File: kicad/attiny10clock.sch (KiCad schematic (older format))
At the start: 45 parts, among them J1 USB_B, SW1 SW_DIP_x01, SW2 SW_DIP_x01, SW3 SW_DIP_x01, SW4 SW_DIP_x01, SW5 SW_DIP_x01, U1 ATtiny10-TS, U2 74HC595, U3 74HC595, U4 74LS247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

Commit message: use different footpritn for osc
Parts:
- X1: footprint Oscillator:Oscillator_SMD_Fordahl_DFAS15-4Pin_5.0x3.2mm -> random_stuff:ASFLK
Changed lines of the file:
@@
 F 0 "X1" H 1644 4296 50  0000 L CNN
 F 1 "DFA-S15" H 1644 4205 50  0000 L CNN
-F 2 "Oscillator:Oscillator_SMD_Fordahl_DFAS15-4Pin_5.0x3.2mm" H 2300 3900 50  0001 C CNN
+F 2 "random_stuff:ASFLK" H 2300 3900 50  0001 C CNN
 F 3 "http://www.metatech.com.hk/product/fordahl/pdf/2002%20TCXO%20Page%2043-58.pdf" H 1100 4250 50  0001 C CNN
 	1    1200 4250

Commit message: Rev 3 of schematic, start pcb
also new code rev
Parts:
- removed C10, C9: 100n, Capacitor_SMD:C_0805_2012Metric_Pad1.15x1.40mm_HandSolder, symbol Device:C
- removed R6: 270, Resistor_SMD:R_1210_3225Metric_Pad1.42x2.65mm_HandSolder, symbol Device:R
- removed U2, U3: 74HC595, Package_SO:SOIC-16_3.9x9.9mm_P1.27mm, symbol 74xx:74HC595
- removed U4, U5, U6, U7: 74LS247, Package_SO:SOIC-16_3.9x9.9mm_P1.27mm, symbol 74xx:74LS247
- added F1: 500ma, Fuse:Fuse_1206_3216Metric_Pad1.42x1.75mm_HandSolder, symbol Device:Fuse
- added J2: Conn_02x04_Odd_Even, Connector_PinHeader_2.54mm:PinHeader_2x04_P2.54mm_Vertical, symbol Connector_Generic:Conn_02x04_Odd_Even
- added U2, U3, U4, U5: NPIC6C595, Package_SO:TSSOP-16_4.4x5mm_P0.65mm, symbol random_things:NPIC6C595
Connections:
- net labels removed: hourha, hourhb, hourla, hourlb, hourlc, hourld, minha, minhb, minhc, minla, minlb, minlc, minld
- wire segments 120 -> 149
- no-connect marks 13 -> 10
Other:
- moved on the sheet: C11, C13, D1, D2, D3, R7, R8, R9, SW1

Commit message: Úse another buck converter
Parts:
- removed C11: 470p, Capacitor_SMD:C_0805_2012Metric_Pad1.15x1.40mm_HandSolder, symbol Device:C
- removed C12: 180u, Capacitor_THT:CP_Radial_D8.0mm_P3.50mm, symbol Device:CP
- removed C13: 100n, Capacitor_SMD:C_0805_2012Metric_Pad1.15x1.40mm_HandSolder, symbol Device:C
- removed C2: 1u, Capacitor_SMD:C_0805_2012Metric_Pad1.15x1.40mm_HandSolder, symbol Device:C
- removed C6: 100u, Capacitor_THT:CP_Radial_D8.0mm_P3.50mm, symbol Device:CP
- removed D7: D_Schottky, Diode_SMD:D_3220_8050Metric_Pad2.65x5.15mm_HandSolder, symbol Device:D_Schottky
- removed L1: 100u, Inductor_THT:L_Toroid_Vertical_L13.0mm_W6.5mm_P5.60mm, symbol Device:L
- removed R7: 150m, Resistor_THT:R_Axial_DIN0309_L9.0mm_D3.2mm_P12.70mm_Horizontal, symbol Device:R
- removed R8: 5k6, Resistor_SMD:R_0603_1608Metric_Pad1.05x0.95mm_HandSolder, symbol Device:R
- removed R9: 3k3, Resistor_SMD:R_0603_1608Metric_Pad1.05x0.95mm_HandSolder, symbol Device:R
- removed U8: MC34063AP, Package_DIP:DIP-8_W7.62mm, symbol Regulator_Switching:MC34063AP
- added C6, C9: 22u, Capacitor_SMD:C_0805_2012Metric_Pad1.15x1.40mm_HandSolder, symbol Device:C_Small
- added L1: 1.5u, Inductor_SMD:L_Wuerth_WE-PD-Typ-7345, symbol Device:L_Small
- added R6: 27k, Resistor_SMD:R_0603_1608Metric_Pad1.05x0.95mm_HandSolder, symbol Device:R_Small
- added R7: 12k, Resistor_SMD:R_0603_1608Metric_Pad1.05x0.95mm_HandSolder, symbol Device:R_Small
- added U6: RT8097AHGB, Package_TO_SOT_SMD:SOT-23-5_HandSoldering, symbol random_things:RT8097AHGB
- R1: value 100 -> 22k
- R2: value 300 -> 10k
- R3: value 1k -> 3k9
- R4: value 3k -> 1k2
- R5: value 1k -> 10k
- SW2, SW3, SW4, SW5: footprint Connector_PinHeader_2.54mm:PinHeader_1x02_P2.54mm_Vertical -> Button_Switch_Keyboard:SW_Cherry_MX_1.00u_Plate
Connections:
- net labels added: btn_in, clk, ser_clk, ser_in
- wire segments 149 -> 120
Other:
- note added: "buttons at \n1.5V, 2.5V, 3.5V 4.5V\n\nshould add thresholds at \n1V 2V 3V 4V\n\nneeds software debounce"
- moved on the sheet: C1, C3, C4, C5, C7, C8, D1, D2, D3, D4, D5, D6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

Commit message: Use new micro usb + more routing
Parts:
- removed J1: USB_B, Connector_USB:USB_B_OST_USB-B1HSxx_Horizontal, symbol Connector:USB_B
- added H1, H2, H3, H4: MountingHole, MountingHole:MountingHole_2.2mm_M2, symbol Mechanical:MountingHole
- added J1: USB_B_Micro, random_stuff:USB_MICRO_10118193-0001LF, symbol Connector:USB_B_Micro
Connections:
- wire segments 120 -> 118
- no-connect marks 10 -> 12
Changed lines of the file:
@@
-	1    0    0    -1
-$EndComp
-$Comp
-L Connector:USB_B J1
-U 1 1 6029C5DE
-P 1200 2750
-F 0 "J1" H 1257 3217 50  0000 C CNN
-F 1 "USB_B" H 1257 3126 50  0000 C CNN
-F 2 "Connector_USB:USB_B_OST_USB-B1HSxx_Horizontal" H 1350 2700 50  0001 C CNN
-F 3 " ~" H 1350 2700 50  0001 C CNN
-	1    1200 2750
 	1    0    0    -1
 $EndComp
@@
 	1    0    0    -1
 $EndComp
-Connection ~ 1200 3150
 Wire Wire Line
 	2500 2550 2500 2450
@@
 	1    0    0    -1
 $EndComp
-Wire Wire Line
-	1200 3150 1100 3150
-$Comp
-L power:GND #PWR0109
-U 1 1 602A0375
-P 1200 3200
-F 0 "#PWR0109" H 1200 2950 50  0001 C CNN
-F 1 "GND" H 1205 3027 50  0000 C CNN
-F 2 "" H 1200 3200 50  0001 C CNN
-F 3 "" H 1200 3200 50  0001 C CNN
-	1    1200 3200
-	1    0    0    -1
-$EndComp
-Wire Wire Line
-	1200 3200 1200 3150
 Wire Wire Line
 	8400 5450 8400 5550
@@
 Text Notes 1200 6300 0    50   ~ 0
 buttons at \n1.5V, 2.5V, 3.5V 4.5V\n\nshould add thresholds at \n1V 2V 3V 4V\n\nneeds software debounce
+$Comp
+L Connector:USB_B_Micro J1
+U 1 1 604EBE7D
+P 1200 2750
+F 0 "J1" H 1257 3217 50  0000 C CNN
+F 1 "USB_B_Micro" H 1257 3126 50  0000 C CNN
+F 2 "random_stuff:USB_MICRO_10118193-0001LF" H 1350 2700 50  0001 C CNN
+F 3 "~" H 1350 2700 50  0001 C CNN
+	1    1200 2750
+	1    0    0    -1
+$EndComp
+NoConn ~ 1500 2950
+$Comp
+L power:GND #PWR0102
+U 1 1 604FD081
+P 1200 3150
+F 0 "#PWR0102" H 1200 2900 50  0001 C CNN
+F 1 "GND" H 1205 2977 50  0000 C CNN
+F 2 "" H 1200 3150 50  0001 C CNN
+F 3 "" H 1200 3150 50  0001 C CNN
+	1    1200 3150
+	1    0    0    -1
+$EndComp
+NoConn ~ 1100 3150
+$Comp
+L Mechanical:MountingHole H1
+U 1 1 6052C894
+P 1350 1000
+F 0 "H1" H 1450 1046 50  0000 L CNN
+F 1 "MountingHole" H 1450 955 50  0000 L CNN
+F 2 "MountingHole:MountingHole_2.2mm_M2" H 1350 1000 50  0001 C CNN
+F 3 "~" H 1350 1000 50  0001 C CNN
+	1    1350 1000
+	1    0    0    -1
+$EndComp
+$Comp
+L Mechanical:MountingHole H2
+U 1 1 6052D0D2
+P 1350 1200
+F 0 "H2" H 1450 1246 50  0000 L CNN
+F 1 "MountingHole" H 1450 1155 50  0000 L CNN
+F 2 "MountingHole:MountingHole_2.2mm_M2" H 1350 1200 50  0001 C CNN
+F 3 "~" H 1350 1200 50  0001 C CNN
+	1    1350 1200
+	1    0    0    -1
+$EndComp
+$Comp
+L Mechanical:MountingHole H3
+U 1 1 6052D545
+P 1350 1400
+F 0 "H3" H 1450 1446 50  0000 L CNN
+F 1 "MountingHole" H 1450 1355 50  0000 L CNN
+F 2 "MountingHole:MountingHole_2.2mm_M2" H 1350 1400 50  0001 C CNN
+F 3 "~" H 1350 1400 50  0001 C CNN
+	1    1350 1400
+	1    0    0    -1
+$EndComp
+$Comp
+L Mechanical:MountingHole H4
+U 1 1 6052D6A0
+P 1350 1600
+F 0 "H4" H 1450 1646 50  0000 L CNN
+F 1 "MountingHole" H 1450 1555 50  0000 L CNN
+F 2 "MountingHole:MountingHole_2.2mm_M2" H 1350 1600 50  0001 C CNN
+F 3 "~" H 1350 1600 50  0001 C CNN
+	1    1350 1600
+	1    0    0    -1
+$EndComp
 $EndSCHEMATC

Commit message: Finalize rev 2 pcb
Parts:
- removed H1, H2, H3, H4: MountingHole, MountingHole:MountingHole_2.2mm_M2, symbol Mechanical:MountingHole
- added H1, H2, H4: MountingHole_Pad, MountingHole:MountingHole_2.2mm_M2_Pad, symbol Mechanical:MountingHole_Pad
- added TP1: TestPoint, TestPoint:TestPoint_Pad_D2.0mm, symbol Connector:TestPoint
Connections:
- net 2v: now also TP1.1
- net GND: now also H1.1, H2.1, H4.1
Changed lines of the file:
@@
 	1    0    0    -1
 $EndComp
-Wire Wire Line
-	4650 5450 5050 5450
 Connection ~ 4650 5450
 Text GLabel 4700 2350 2    50   Input ~ 0
@@
 NoConn ~ 1100 3150
 $Comp
-L Mechanical:MountingHole H1
-U 1 1 6052C894
-P 1350 1000
-F 0 "H1" H 1450 1046 50  0000 L CNN
-F 1 "MountingHole" H 1450 955 50  0000 L CNN
-F 2 "MountingHole:MountingHole_2.2mm_M2" H 1350 1000 50  0001 C CNN
-F 3 "~" H 1350 1000 50  0001 C CNN
-	1    1350 1000
-	1    0    0    -1
-$EndComp
-$Comp
-L Mechanical:MountingHole H2
-U 1 1 6052D0D2
-P 1350 1200
-F 0 "H2" H 1450 1246 50  0000 L CNN
-F 1 "MountingHole" H 1450 1155 50  0000 L CNN
-F 2 "MountingHole:MountingHole_2.2mm_M2" H 1350 1200 50  0001 C CNN
-F 3 "~" H 1350 1200 50  0001 C CNN
-	1    1350 1200
-	1    0    0    -1
-$EndComp
-$Comp
-L Mechanical:MountingHole H3
-U 1 1 6052D545
-P 1350 1400
-F 0 "H3" H 1450 1446 50  0000 L CNN
-F 1 "MountingHole" H 1450 1355 50  0000 L CNN
-F 2 "MountingHole:MountingHole_2.2mm_M2" H 1350 1400 50  0001 C CNN
-F 3 "~" H 1350 1400 50  0001 C CNN
-	1    1350 1400
-	1    0    0    -1
-$EndComp
-$Comp
-L Mechanical:MountingHole H4
-U 1 1 6052D6A0
-P 1350 1600
-F 0 "H4" H 1450 1646 50  0000 L CNN
-F 1 "MountingHole" H 1450 1555 50  0000 L CNN
-F 2 "MountingHole:MountingHole_2.2mm_M2" H 1350 1600 50  0001 C CNN
-F 3 "~" H 1350 1600 50  0001 C CNN
-	1    1350 1600
-	1    0    0    -1
-$EndComp
+L Connector:TestPoint TP1
+U 1 1 6051D169
+P 10100 1350
+F 0 "TP1" H 10158 1468 50  0000 L CNN
+F 1 "TestPoint" H 10158 1377 50  0000 L CNN
+F 2 "TestPoint:TestPoint_Pad_D2.0mm" H 10300 1350 50  0001 C CNN
+F 3 "~" H 10300 1350 50  0001 C CNN
+	1    10100 1350
+	-1   0    0    1
+$EndComp
+Text GLabel 10100 1350 1    50   Input ~ 0
+2v
+Wire Wire Line
+	4650 5450 5050 5450
+$Comp
+L Mechanical:MountingHole_Pad H1
+U 1 1 60530F90
+P 10050 1900
+F 0 "H1" V 10004 2050 50  0000 L CNN
+F 1 "MountingHole_Pad" V 10095 2050 50  0000 L CNN
+F 2 "MountingHole:MountingHole_2.2mm_M2_Pad" H 10050 1900 50  0001 C CNN
+F 3 "~" H 10050 1900 50  0001 C CNN
+	1    10050 1900
+	0    1    1    0
+$EndComp
+$Comp
+L Mechanical:MountingHole_Pad H2
+U 1 1 60531C39
+P 10050 2100
+F 0 "H2" V 10004 2250 50  0000 L CNN
+F 1 "MountingHole_Pad" V 10095 2250 50  0000 L CNN
+F 2 "MountingHole:MountingHole_2.2mm_M2_Pad" H 10050 2100 50  0001 C CNN
+F 3 "~" H 10050 2100 50  0001 C CNN
+	1    10050 2100
+	0    1    1    0
+$EndComp
+$Comp
+L Mechanical:MountingHole_Pad H4
+U 1 1 60531F46
+P 10050 2500
+F 0 "H4" V 10004 2650 50  0000 L CNN
+F 1 "MountingHole_Pad" V 10095 2650 50  0000 L CNN
+F 2 "MountingHole:MountingHole_2.2mm_M2_Pad" H 10050 2500 50  0001 C CNN
+F 3 "~" H 10050 2500 50  0001 C CNN
+	1    10050 2500
+	0    1    1    0
+$EndComp
+Wire Wire Line
+	9950 1900 9950 2100
+Connection ~ 9950 2100
+$Comp
+L power:GND #PWR0103
+U 1 1 605410CB
+P 9950 2600
+F 0 "#PWR0103" H 9950 2350 50  0001 C CNN
+F 1 "GND" H 9955 2427 50  0000 C CNN
+F 2 "" H 9950 2600 50  0001 C CNN
+F 3 "" H 9950 2600 50  0001 C CNN
+	1    9950 2600
+	1    0    0    -1
+$EndComp
+Wire Wire Line
+	9950 2600 9950 2500
+Connection ~ 9950 2500
+Wire Wire Line
+	9950 2100 9950 2500
 $EndSCHEMATC

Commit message: Yey hardware works
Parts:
- D3, D4, D5, D6: symbol random_things:SA56-11EWA -> attiny10clock-rescue:SA56-11EWA-random_things
- U2, U3, U4, U5: symbol random_things:NPIC6C595 -> attiny10clock-rescue:NPIC6C595-random_things
- U6: symbol random_things:RT8097AHGB -> attiny10clock-rescue:RT8097AHGB-random_things
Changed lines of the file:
@@
 	8400 1400 8400 1500
 $Comp
-L random_things:SA56-11EWA D6
+L attiny10clock-rescue:SA56-11EWA-random_things D6
 U 1 1 604BC073
 P 8150 5800
@@
 NoConn ~ 7800 6150
 $Comp
-L random_things:NPIC6C595 U5
+L attiny10clock-rescue:NPIC6C595-random_things U5
 U 1 1 604BC068
 P 7450 5900
@@
 	7800 5450 7900 5450
 $Comp
-L random_things:SA56-11EWA D5
+L attiny10clock-rescue:SA56-11EWA-random_things D5
 U 1 1 604B56B5
 P 8150 4450
@@
 NoConn ~ 7800 4800
 $Comp
-L random_things:NPIC6C595 U4
+L attiny10clock-rescue:NPIC6C595-random_things U4
 U 1 1 604B56AA
 P 7450 4550
@@
 	7800 4100 7900 4100
 $Comp
-L random_things:SA56-11EWA D4
+L attiny10clock-rescue:SA56-11EWA-random_things D4
 U 1 1 604B2662
 P 8150 3100
@@
 NoConn ~ 7900 3450
 $Comp
-L random_things:NPIC6C595 U3
+L attiny10clock-rescue:NPIC6C595-random_things U3
 U 1 1 604B2657
 P 7450 3200
@@
 	7800 2750 7900 2750
 $Comp
-L random_things:SA56-11EWA D3
+L attiny10clock-rescue:SA56-11EWA-random_things D3
 U 1 1 6036F5A5
 P 8150 1750
@@
 NoConn ~ 7800 2100
 $Comp
-L random_things:NPIC6C595 U2
+L attiny10clock-rescue:NPIC6C595-random_things U2
 U 1 1 60492F39
 P 7450 1850
@@
 $EndComp
 $Comp
-L random_things:RT8097AHGB U6
+L attiny10clock-rescue:RT8097AHGB-random_things U6
 U 1 1 6059CE26
 P 4150 5550

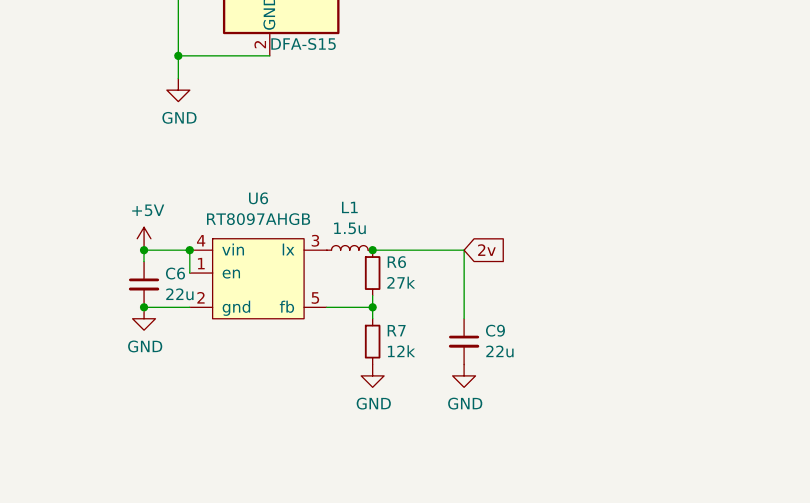
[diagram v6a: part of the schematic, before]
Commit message: Lower led voltage
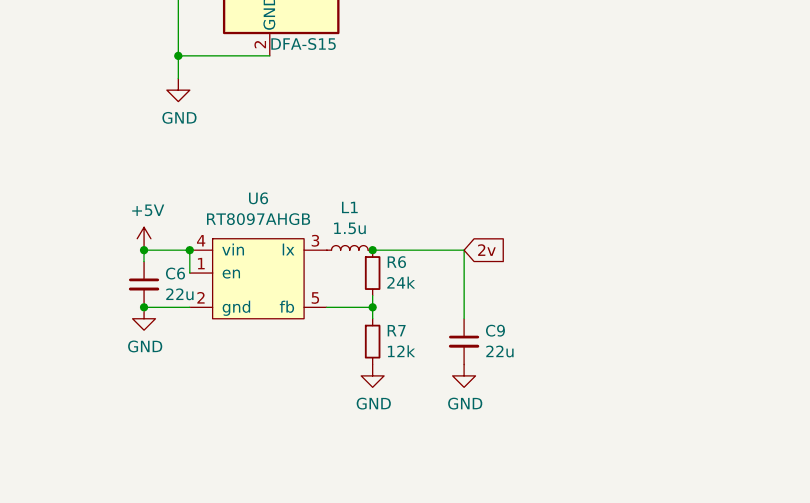
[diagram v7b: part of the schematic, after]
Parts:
- R6: value 27k -> 24k
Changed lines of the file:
@@
 P 4650 5550
 F 0 "R6" H 4709 5596 50  0000 L CNN
-F 1 "27k" H 4709 5505 50  0000 L CNN
+F 1 "24k" H 4709 5505 50  0000 L CNN
 F 2 "Resistor_SMD:R_0603_1608Metric_Pad1.05x0.95mm_HandSolder" H 4650 5550 50  0001 C CNN
 F 3 "~" H 4650 5550 50  0001 C CNN

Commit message: Code is DONW
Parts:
- D3, D4, D5, D6: symbol attiny10clock-rescue:SA56-11EWA-random_things -> attiny10clock-rescue:SA56-11EWA-random_things-attiny10clock-rescue
- U2, U3, U4, U5: symbol attiny10clock-rescue:NPIC6C595-random_things -> attiny10clock-rescue:NPIC6C595-random_things-attiny10clock-rescue
- U6: symbol attiny10clock-rescue:RT8097AHGB-random_things -> attiny10clock-rescue:RT8097AHGB-random_things-attiny10clock-rescue
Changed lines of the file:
@@
 	8400 1400 8400 1500
 $Comp
-L attiny10clock-rescue:SA56-11EWA-random_things D6
+L attiny10clock-rescue:SA56-11EWA-random_things-attiny10clock-rescue D6
 U 1 1 604BC073
 P 8150 5800
@@
 NoConn ~ 7800 6150
 $Comp
-L attiny10clock-rescue:NPIC6C595-random_things U5
+L attiny10clock-rescue:NPIC6C595-random_things-attiny10clock-rescue U5
 U 1 1 604BC068
 P 7450 5900
@@
 	7800 5450 7900 5450
 $Comp
-L attiny10clock-rescue:SA56-11EWA-random_things D5
+L attiny10clock-rescue:SA56-11EWA-random_things-attiny10clock-rescue D5
 U 1 1 604B56B5
 P 8150 4450
@@
 NoConn ~ 7800 4800
 $Comp
-L attiny10clock-rescue:NPIC6C595-random_things U4
+L attiny10clock-rescue:NPIC6C595-random_things-attiny10clock-rescue U4
 U 1 1 604B56AA
 P 7450 4550
@@
 	7800 4100 7900 4100
 $Comp
-L attiny10clock-rescue:SA56-11EWA-random_things D4
+L attiny10clock-rescue:SA56-11EWA-random_things-attiny10clock-rescue D4
 U 1 1 604B2662
 P 8150 3100
@@
 NoConn ~ 7900 3450
 $Comp
-L attiny10clock-rescue:NPIC6C595-random_things U3
+L attiny10clock-rescue:NPIC6C595-random_things-attiny10clock-rescue U3
 U 1 1 604B2657
 P 7450 3200
@@
 	7800 2750 7900 2750
 $Comp
-L attiny10clock-rescue:SA56-11EWA-random_things D3
+L attiny10clock-rescue:SA56-11EWA-random_things-attiny10clock-rescue D3
 U 1 1 6036F5A5
 P 8150 1750
@@
 NoConn ~ 7800 2100
 $Comp
-L attiny10clock-rescue:NPIC6C595-random_things U2
+L attiny10clock-rescue:NPIC6C595-random_things-attiny10clock-rescue U2
 U 1 1 60492F39
 P 7450 1850
@@
 $EndComp
 $Comp
-L attiny10clock-rescue:RT8097AHGB-random_things U6
+L attiny10clock-rescue:RT8097AHGB-random_things-attiny10clock-rescue U6
 U 1 1 6059CE26
 P 4150 5550
